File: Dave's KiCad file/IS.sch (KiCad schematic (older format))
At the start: 0 parts

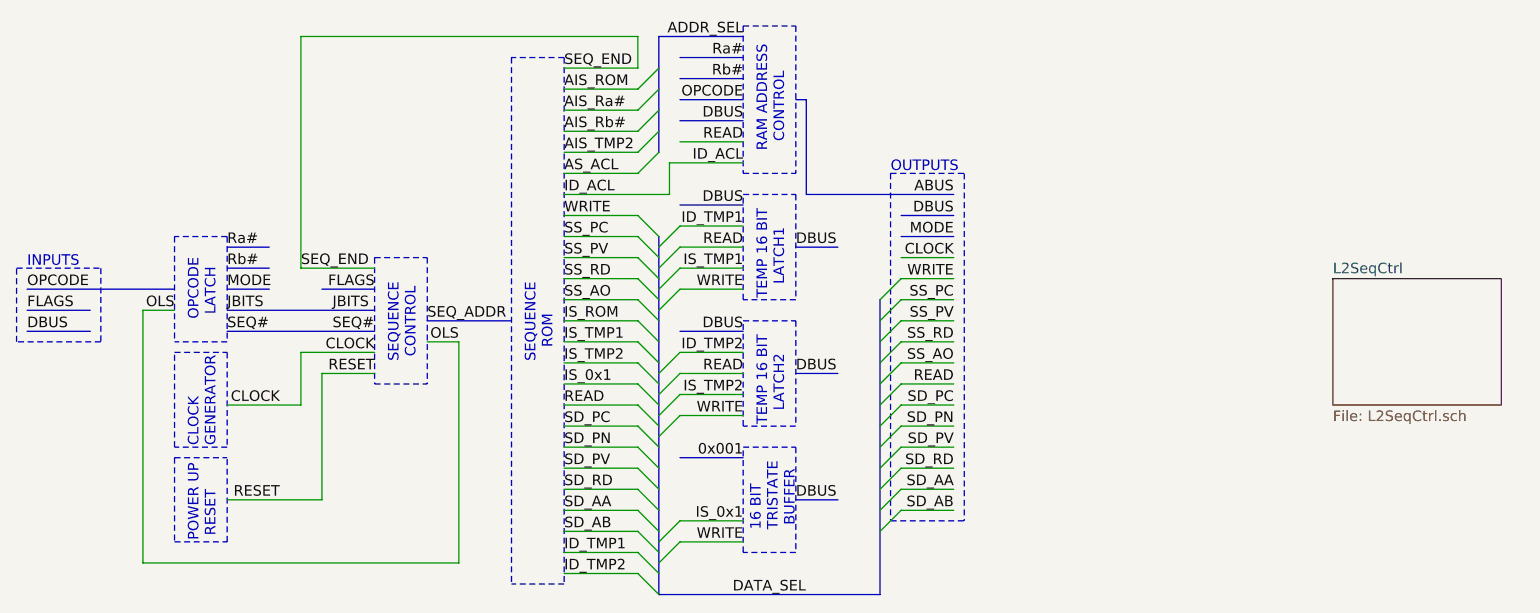
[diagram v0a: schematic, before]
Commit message: Remove READ and WRITE
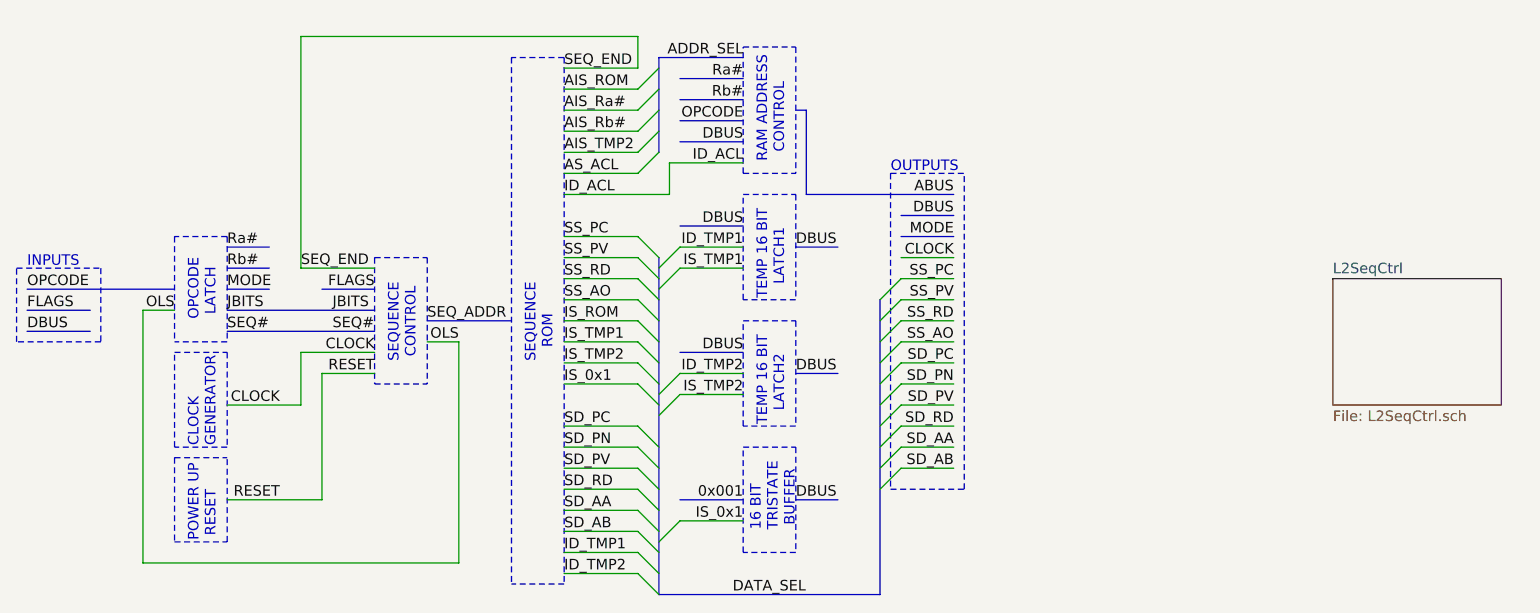
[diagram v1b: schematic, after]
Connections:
- net labels removed: READ, WRITE
- wire segments 66 -> 56
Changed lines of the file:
@@
 Text Label 2300 3200 0    50   ~ 0
 Rb#
-Text Label 3900 2950 0    50   ~ 0
-WRITE
 Text Label 3900 3050 0    50   ~ 0
 SS_PC
@@
 Text Label 3900 3350 0    50   ~ 0
 SS_AO
-Text Label 3900 3850 0    50   ~ 0
-READ
 Text Label 3900 3950 0    50   ~ 0
 SD_PC
@@
 	3900 2750 4250 2750
 Wire Wire Line
-	3900 2950 4250 2950
-Wire Wire Line
 	3900 3050 4250 3050
 Wire Wire Line
@@
 Wire Wire Line
 	3900 3750 4250 3750
-Wire Wire Line
-	3900 3850 4250 3850
 Wire Wire Line
 	3900 3950 4250 3950
@@
 	3900 4650 4250 4650
 Entry Wire Line
-	4250 2950 4350 3050
-Entry Wire Line
 	4250 3050 4350 3150
 Entry Wire Line
@@
 Entry Wire Line
 	4250 3750 4350 3850
-Entry Wire Line
-	4250 3850 4350 3950
 Entry Wire Line
 	4250 3950 4350 4050
@@
 Entry Wire Line
 	4250 2350 4350 2250
-Text Notes 4950 2650 1    50   ~ 0
+Text Notes 4950 2700 1    50   ~ 0
 RAM ADDRESS\n  CONTROL
-Text Label 4750 2100 2    50   ~ 0
+Text Label 4750 2200 2    50   ~ 0
 ADDR_SEL
+Text Label 4750 2600 2    50   ~ 0
+DBUS
 Text Label 4750 2500 2    50   ~ 0
-DBUS
+OPCODE
+Wire Bus Line
+	4750 2500 4450 2500
+Text Label 4750 2300 2    50   ~ 0
+Ra#
 Text Label 4750 2400 2    50   ~ 0
-OPCODE
-Wire Bus Line
-	4750 2400 4450 2400
-Text Label 4750 2200 2    50   ~ 0
-Ra#
-Text Label 4750 2300 2    50   ~ 0
 Rb#
 Wire Bus Line
+	4450 2400 4750 2400
+Wire Bus Line
 	4450 2300 4750 2300
-Wire Bus Line
-	4450 2200 4750 2200
 Wire Wire Line
 	3400 3550 3250 3550
@@
 Text Notes 4950 3350 1    50   ~ 0
 TEMP 16 BIT\n   LATCH1
-Text Label 4750 2900 2    50   ~ 0
-DBUS
-Wire Bus Line
-	4450 2900 4750 2900
+Text Label 4750 3000 2    50   ~ 0
+DBUS
+Wire Bus Line
+	4450 3000 4750 3000
 Wire Bus Line
 	5000 3100 5200 3100
@@
 DBUS
 Wire Wire Line
-	4750 3000 4450 3000
-Text Label 4750 3000 2    50   ~ 0
+	4750 3100 4450 3100
+Text Label 4750 3100 2    50   ~ 0
 ID_TMP1
-Text Label 4750 3100 2    50   ~ 0
-READ
-Wire Wire Line
-	4450 3100 4750 3100
 Wire Wire Line
 	4750 3200 4450 3200
 Text Label 4750 3200 2    50   ~ 0
 IS_TMP1
-Text Label 4750 3300 2    50   ~ 0
-WRITE
-Wire Wire Line
-	4450 3300 4750 3300
 Wire Notes Line style solid rgb(0, 255, 0)
 	4750 2850 5000 2850
@@
 Wire Notes Line style solid rgb(0, 255, 0)
 	5000 3350 4750 3350
-Wire Notes Line
-	5800 2750 5800 4400
-Wire Notes Line
-	5450 2750 5450 4400
 Wire Notes Line
 	5450 2750 5800 2750
@@
 ABUS
 Entry Wire Line
-	5400 4450 5500 4350
-Entry Wire Line
-	5400 4350 5500 4250
-Entry Wire Line
 	5400 4250 5500 4150
 Entry Wire Line
@@
 Text Notes 5450 2750 0    50   ~ 0
 OUTPUTS
-Wire Notes Line
-	5450 4400 5800 4400
 Text Label 5750 3050 2    50   ~ 0
 MODE
@@
 	5500 3050 5750 3050
 Wire Wire Line
-	5750 4350 5500 4350
-Text Label 5750 4350 2    50   ~ 0
-SD_AB
-Wire Wire Line
-	5750 4250 5500 4250
-Text Label 5750 4250 2    50   ~ 0
-SD_AA
-Wire Wire Line
 	5750 4150 5500 4150
 Text Label 5750 4150 2    50   ~ 0
-SD_RD
+SD_AB
 Wire Wire Line
 	5750 4050 5500 4050
 Text Label 5750 4050 2    50   ~ 0
-SD_PV
+SD_AA
 Wire Wire Line
 	5750 3950 5500 3950
 Text Label 5750 3950 2    50   ~ 0
-SD_PN
+SD_RD
 Wire Wire Line
 	5750 3850 5500 3850
 Text Label 5750 3850 2    50   ~ 0
-SD_PC
+SD_PV
 Wire Wire Line
 	5750 3750 5500 3750
 Text Label 5750 3750 2    50   ~ 0
-READ
+SD_PN
 Wire Wire Line
 	5750 3650 5500 3650
 Text Label 5750 3650 2    50   ~ 0
-SS_AO
+SD_PC
 Wire Wire Line
 	5750 3550 5500 3550
 Text Label 5750 3550 2    50   ~ 0
-SS_RD
+SS_AO
 Wire Wire Line
 	5750 3450 5500 3450
 Text Label 5750 3450 2    50   ~ 0
-SS_PV
+SS_RD
 Wire Wire Line
 	5750 3350 5500 3350
 Text Label 5750 3350 2    50   ~ 0
+SS_PV
+Wire Wire Line
+	5750 3250 5500 3250
+Text Label 5750 3250 2    50   ~ 0
 SS_PC
 Wire Wire Line
-	5750 3250 5500 3250
-Wire Wire Line
 	5500 3150 5750 3150
-Text Label 5750 3250 2    50   ~ 0
-WRITE
 Text Label 5750 3150 2    50   ~ 0
 CLOCK
@@
 	4750 3350 4750 2850
 Entry Wire Line
-	4350 3100 4450 3000
-Entry Wire Line
 	4350 3200 4450 3100
 Entry Wire Line
 	4350 3300 4450 3200
-Entry Wire Line
-	4350 3400 4450 3300
 Text Notes 4950 3950 1    50   ~ 0
 TEMP 16 BIT\n   LATCH2
-Text Label 4750 3500 2    50   ~ 0
-DBUS
-Wire Bus Line
-	4450 3500 4750 3500
+Text Label 4750 3600 2    50   ~ 0
+DBUS
+Wire Bus Line
+	4450 3600 4750 3600
 Wire Bus Line
 	5000 3700 5200 3700
@@
 DBUS
 Wire Wire Line
-	4750 3600 4450 3600
-Text Label 4750 3600 2    50   ~ 0
+	4750 3700 4450 3700
+Text Label 4750 3700 2    50   ~ 0
 ID_TMP2
-Text Label 4750 3700 2    50   ~ 0
-READ
-Wire Wire Line
-	4450 3700 4750 3700
 Wire Wire Line
 	4750 3800 4450 3800
 Text Label 4750 3800 2    50   ~ 0
 IS_TMP2
-Text Label 4750 3900 2    50   ~ 0
-WRITE
-Wire Wire Line
-	4450 3900 4750 3900
 Wire Notes Line style solid rgb(0, 255, 0)
 	4750 3450 5000 3450
@@
 	4750 3950 4750 3450
 Entry Wire Line
-	4350 3700 4450 3600
-Entry Wire Line
 	4350 3800 4450 3700
-Entry Wire Line
-	4350 3900 4450 3800
-Entry Wire Line
-	4350 4000 4450 3900
 Text Notes 5000 4450 1    50   ~ 0
  16 BIT \nTRISTATE\n BUFFER
-Text Label 4750 4100 2    50   ~ 0
+Text Label 4750 4300 2    50   ~ 0
 0x001
 Wire Bus Line
-	4450 4100 4750 4100
+	4450 4300 4750 4300
 Wire Bus Line
 	5000 4300 5200 4300
@@
 Text Label 4750 4400 2    50   ~ 0
 IS_0x1
-Text Label 4750 4500 2    50   ~ 0
-WRITE
-Wire Wire Line
-	4450 4500 4750 4500
 Wire Notes Line style solid rgb(0, 255, 0)
 	4750 4050 5000 4050
@@
 Entry Wire Line
 	4350 4500 4450 4400
-Entry Wire Line
-	4350 4600 4450 4500
 Wire Bus Line
 	4350 4750 5400 4750
@@
 Wire Notes Line style solid rgb(0, 255, 0)
 	3000 3150 3000 3750
-Text Label 4750 2600 2    50   ~ 0
-READ
-Wire Wire Line
-	4450 2600 4750 2600
 Text Label 3900 2850 0    50   ~ 0
 ID_ACL
 Wire Bus Line
-	4750 2500 4450 2500
-Wire Notes Line style solid rgb(0, 255, 0)
-	4750 2050 5000 2050
-Wire Bus Line
-	4350 2100 4750 2100
+	4750 2600 4450 2600
+Wire Bus Line
+	4350 2200 4750 2200
 Wire Bus Line
 	5050 2850 5750 2850
@@
 Wire Notes Line style solid rgb(0, 255, 0)
 	3650 2200 3650 4700
-Wire Wire Line
-	3900 2850 4400 2850
-Wire Wire Line
-	4400 2700 4400 2850
-Wire Wire Line
-	4400 2700 4750 2700
 Text Label 4750 2700 2    50   ~ 0
 ID_ACL
 Wire Notes Line style solid rgb(0, 255, 0)
 	4750 2750 5000 2750
-Wire Bus Line
-	5000 2400 5050 2400
-Wire Bus Line
-	5050 2400 5050 2850
-Wire Notes Line style solid rgb(0, 255, 0)
-	4750 2050 4750 2750
-Wire Notes Line style solid rgb(0, 255, 0)
-	5000 2050 5000 2750
 Wire Wire Line
 	3400 3550 3400 4600
@@
 Wire Wire Line
 	1900 4600 1900 3400
-Wire Bus Line
-	4350 2100 4350 2650
-Wire Bus Line
-	5400 3350 5400 4750
-Wire Bus Line
-	4350 3050 4350 4750
 $Sheet
 S 7550 3250 800  600
@@
 F1 "L2SeqCtrl.sch" 50
 $EndSheet
+Entry Wire Line
+	4350 3900 4450 3800
+Wire Notes Line style solid rgb(0, 255, 0)
+	4750 2150 5000 2150
+Wire Notes Line style solid rgb(0, 255, 0)
+	4750 2750 4750 2150
+Wire Notes Line style solid rgb(0, 255, 0)
+	5000 2150 5000 2750
+Wire Bus Line
+	5000 2450 5050 2450
+Wire Bus Line
+	5050 2450 5050 2850
+Wire Wire Line
+	3900 2850 4400 2850
+Wire Wire Line
+	4400 2700 4750 2700
+Wire Wire Line
+	4400 2700 4400 2850
+Wire Notes Line
+	5450 4250 5800 4250
+Wire Notes Line
+	5450 2750 5450 4250
+Wire Notes Line
+	5800 4250 5800 2750
+Wire Bus Line
+	4350 2200 4350 2650
+Wire Bus Line
+	5400 3350 5400 4750
+Wire Bus Line
+	4350 3150 4350 4750
 $EndSCHEMATC
